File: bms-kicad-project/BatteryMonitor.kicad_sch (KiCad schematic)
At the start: 49 parts, among them J2 1053141210, U1 CD74HC4067, U2 BQ7697204PFBR

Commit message: feat: big pre-design review schematic commit
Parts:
- removed J2: 1053141210, FixedWing:CONN_SD-105314-100_10_MOL, symbol FixedWing:1053141210
- added C14: 0.1µ, FixedWing:CAP_GCJ-18_MUR, symbol FixedWing:GCJ188R72A104KA01D
- added C22, C23, C24, C25, C26, C27: 3.9n, FixedWing:G-21_MUR, symbol FixedWing:GRM2165C1H392JA01D
- added J2: 1053141308, FixedWing:CONN_SD-105314-100_08_MOL, symbol FixedWing:1053141308
- renumbered C14 to C15, C15 to C16, C16 to C17, C17 to C18, C18 to C19, C19 to C20, C20 to C21
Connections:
- net +5V: now also C14.2
- net GND: now also C14.1, C22.1, C23.1, C24.1, C25.1, C26.1, C27.1, J2.7, J2.8
- net THERM1: now reaches U2.21 (TS1)
- net THERM1: now also C22.2, J2.1
- net THERM2: now reaches U2.22 (TS2)
- net THERM2: now also C23.2, J2.2
- net THERM3: now reaches U2.23 (TS3)
- net THERM3: now also C24.2, J2.3
- net THERM4: now reaches U2.30 (DFETOFF)
- net THERM4: now also C25.2, J2.4
- net THERM5: now reaches U2.31 (DCHG)
- net THERM5: now also C26.2, J2.5
- net THERM6: now reaches U2.32 (DDSG)
- net THERM6: now also C27.2, J2.6
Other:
- moved on the sheet: C15, C16, C17, C18, C19, C20, C21, D1, NT1, R62, R63, R64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

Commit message: feat: post-design review clarity
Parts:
- added TP1, TP2, TP6, TP7: ~, TestPoint:TestPoint_Pad_D1.0mm, symbol FixedWing:TestPoint
- TP3: renamed from TP1; value TestPoint -> ~; footprint TestPoint:TestPoint_Pad_D1.5mm -> TestPoint:TestPoint_Pad_D1.0mm; symbol Connector:TestPoint -> FixedWing:TestPoint
- TP4: renamed from TP2; value TestPoint -> ~; footprint TestPoint:TestPoint_Pad_D1.5mm -> TestPoint:TestPoint_Pad_D1.0mm; symbol Connector:TestPoint -> FixedWing:TestPoint
- TP5: renamed from TP3; value TestPoint -> ~; footprint TestPoint:TestPoint_Pad_D1.5mm -> TestPoint:TestPoint_Pad_D1.0mm; symbol Connector:TestPoint -> FixedWing:TestPoint
- TP8: renamed from TP4; value TestPoint -> ~; footprint TestPoint:TestPoint_Pad_D1.5mm -> TestPoint:TestPoint_Pad_D1.0mm; symbol Connector:TestPoint -> FixedWing:TestPoint
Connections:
- net C0: now also TP2.1
- net C1: now also TP1.1
- net GND: now also TP6.1
- net at C21.1, U2.24 (REG18): now also TP7.1
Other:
- moved on the sheet: C21

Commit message: feat: I am so tired. 4-layer layout almost done
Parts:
- removed NT1: NetTie_2, NetTie:NetTie-2_SMD_Pad0.5mm, symbol Device:NetTie_2
- removed TP1, TP2, TP5, TP7, TP8: ~, TestPoint:TestPoint_Pad_D1.0mm, symbol FixedWing:TestPoint
- added TP2, TP5: 5261, FixedWing:KEYSTONE_5261, symbol FixedWing:5261
- renumbered TP3 to TP1, TP4 to TP3, TP6 to TP4
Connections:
- net GNDPWR is gone; now on net GND: R92.2, R93.2
- net -BATT: now also TP2.TP
- net GND: now also TP5.TP

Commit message: feat: biiig layout and slight design change commit
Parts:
- removed R69, R70: 10k, FixedWing:KOA_Speer-RK73H2A-0-0-MFG, symbol FixedWing:RK73H2ATTD1002F
- removed R92: 0.5m, FixedWing:RES_3920R, symbol FixedWing:PEWM3920FL500K9
- removed TP1: ~, TestPoint:TestPoint_Pad_D1.0mm, symbol FixedWing:TestPoint
- removed U1: CD74HC4067, FixedWing:DB0024A_N, symbol FixedWing:CD74HC4067
- added C14: 1µ, FixedWing:CAPC1608X90N, symbol FixedWing:GCM188R71C105KA64D
- added R65, R70, R71: 0, FixedWing:RES_CRCW_0805_VIS, symbol FixedWing:CRCW08050000Z0EA
- added R93: 1m, FixedWing:RES_5930R, symbol FixedWing:SEWF5930F1L00P9
- added U1: TMUX7208PWR, FixedWing:TSSOP16-PW_TEX, symbol FixedWing:TMUX7208PWR
- R68: renamed from R67; now not fitted
- R69: renamed from R68; now fitted
- renumbered C14 to C15, C15 to C16, C16 to C17, C17 to C18, C18 to C19, C19 to C20, C20 to C21, C21 to C22, C22 to C23, C23 to C24, C24 to C25, C25 to C26, C26 to C27, C27 to C28, R65 to R66, R66 to R67, R71 to R72, R72 to R73, R73 to R74, R74 to R75, R75 to R76, R76 to R77, R77 to R78, R78 to R79, R79 to R80, R80 to R81, R81 to R82, R82 to R83, R83 to R84, R84 to R85, R85 to R86, R86 to R87, R87 to R88, R88 to R89, R89 to R90, R90 to R91, R91 to R92, R93 to R94, R94 to R95, TP2 to TP1, TP3 to TP2, TP4 to TP3, TP5 to TP4
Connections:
- net +5V is gone; now on net +BATT: C15.2, R63.2, R66.2, R68.2
- net +BATT: now also R62.2, C14.2, U1.13 (VDD)
- net -BATT: now also R93.1
- net C10: now also U1.11 (S6)
- net C11: now also U1.10 (S7)
- net C12: now also U1.9 (S8)
- net C3: now also R71.2
- net C4: now also R70.2
- net C5: now also U1.4 (S1)
- net C6: now also U1.5 (S2)
- net C7: now also U1.6 (S3)
- net C8: now also U1.7 (S4)
- net C9: now also U1.12 (S5)
- net GND: now also C14.1, R93.2, U1.14 (GND), U1.3 (VSS); no longer R62.1
- net at R66.1, R67.1: now also U1.16 (A1)
- net at R63.1, R64.1: now also U1.1 (A0)
- net at U2.48 (VC16): now also R65.2, R70.1, R71.1
- net at R68.1, R69.1: now also U1.15 (A2)
- new net: R65.1, U1.8 (D)
- new net: R62.1, U1.2 (EN)
- no-connect marks 12 -> 6
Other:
- moved on the sheet: C15, C16, C17, C18, C19, C20, C21, C22, C23, C24, C25, C26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

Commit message: feat:bos->lax layout sesh
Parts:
- removed TP2, TP3: ~, TestPoint:TestPoint_Pad_D1.0mm, symbol FixedWing:TestPoint
- added R63: 10k, FixedWing:KOA_Speer-RK73H2A-0-0-MFG, symbol FixedWing:RK73H2ATTD1002F
- renumbered R63 to R64, R64 to R65, R65 to R66, R66 to R67, R67 to R68, R68 to R69, R69 to R70, R70 to R71, R71 to R72, R72 to R73, R73 to R74, R74 to R75, R75 to R76, R76 to R77, R77 to R78, R78 to R79, R79 to R80, R80 to R81, R81 to R82, R82 to R83, R83 to R84, R84 to R85, R85 to R86, R86 to R87, R87 to R88, R88 to R89, R89 to R90, R90 to R91, R91 to R92, R92 to R93, R93 to R94, R94 to R95, R95 to R96, TP4 to TP2
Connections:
- net GND: now also R63.1
- net at R62.1, U1.2 (EN): now also R63.2

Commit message: feat: lax -> syd layout sesh
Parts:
- removed TP1: 5261, FixedWing:KEYSTONE_5261, symbol FixedWing:5261
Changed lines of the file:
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@@
     (company "AeroNU - FixedWing")
   )
-  (junction (at 259.08 207.01) (diameter 0) (color 0 0 0 0)
-  )
   (junction (at 318.77 219.71) (diameter 0) (color 0 0 0 0)
   )
@@
     (stroke (width 0) (type default))
   )
-  (wire (pts (xy 259.08 207.01) (xy 259.08 208.28))
-    (stroke (width 0) (type default))
-  )
   (wire (pts (xy 41.91 245.11) (xy 41.91 246.38))
     (stroke (width 0) (type default))
@@
     (stroke (width 0) (type default))
   )
-  (wire (pts (xy 259.08 207.01) (xy 271.78 207.01))
-    (stroke (width 0) (type default))
-  )
   (polyline (pts (xy 29.21 138.43) (xy 44.45 138.43))
     (stroke (width 0) (type default))
@@
     (stroke (width 0) (type default))
   )
-  (wire (pts (xy 248.92 207.01) (xy 259.08 207.01))
+  (wire (pts (xy 248.92 207.01) (xy 271.78 207.01))
     (stroke (width 0) (type default))
   )
@@
         )
       )
-    )
-  )
-  (symbol (lib_id "FixedWing:5261") (at 259.08 213.36 270) (unit 1)
-    (in_bom yes) (on_board yes) (dnp no)
-    (property "Reference" "TP1" (at 256.54 215.9 90)
-      (effects (font (size 1.27 1.27)) (justify left))
-    )
-    (property "Value" "5261" (at 253.9934 210.81 0)
-      (effects (font (size 1.27 1.27)) (justify left bottom) hide)
-    )
-    (property "Footprint" "FixedWing:KEYSTONE_5261" (at 259.08 213.36 0)
-      (effects (font (size 1.27 1.27)) (justify bottom) hide)
-    )
-    (property "Datasheet" "https://www.keyelco.com/product-pdf.cfm?p=14608" (at 259.08 213.36 0)
-      (effects (font (size 1.27 1.27)) hide)
-    )
-    (property "PARTREV" "H" (at 259.08 213.36 0)
-      (effects (font (size 1.27 1.27)) (justify bottom) hide)
-    )
-    (property "STANDARD" "Manufacturer Recommendations" (at 259.08 213.36 0)
-      (effects (font (size 1.27 1.27)) (justify bottom) hide)
-    )
-    (property "SNAPEDA_PN" "5000" (at 259.08 213.36 0)
-      (effects (font (size 1.27 1.27)) (justify bottom) hide)
-    )
-    (property "MAXIMUM_PACKAGE_HEIGHT" "4.57 mm" (at 259.08 213.36 0)
-      (effects (font (size 1.27 1.27)) (justify bottom) hide)
-    )
-    (property "Manufacturer" "Keystone" (at 259.08 213.36 0)
-      (effects (font (size 1.27 1.27)) (justify bottom) hide)
-    )
-    (property "Manufacturer Part Number" "5261" (at 259.08 213.36 0)
-      (effects (font (size 1.27 1.27)) hide)
-    )
-    (pin "TP")
-    (instances
-      (project "bms-board"
-        (path "/8a7831d1-a913-4f04-8780-225d2234b41d/1e9f81b4-c330-4dde-84b6-9168ce482c70"
-          (reference "TP1") (unit 1)
-        )
-      )

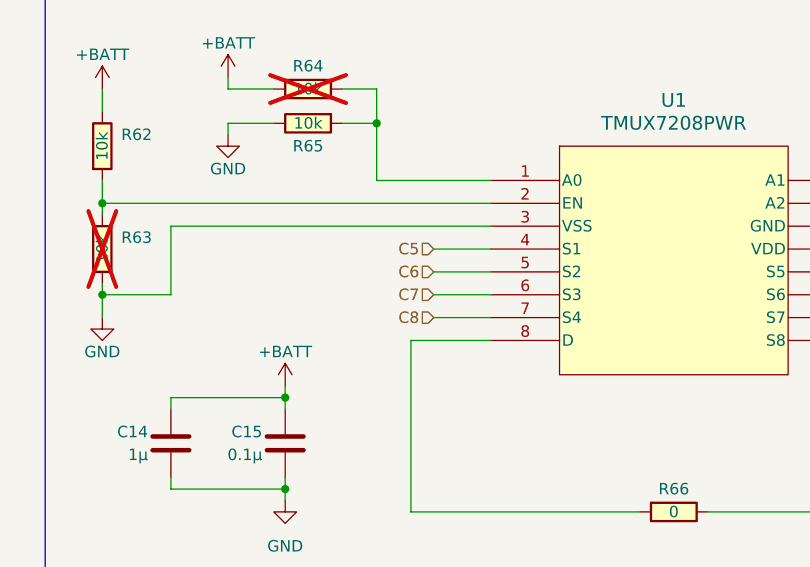
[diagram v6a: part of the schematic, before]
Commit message: feat: DRC run
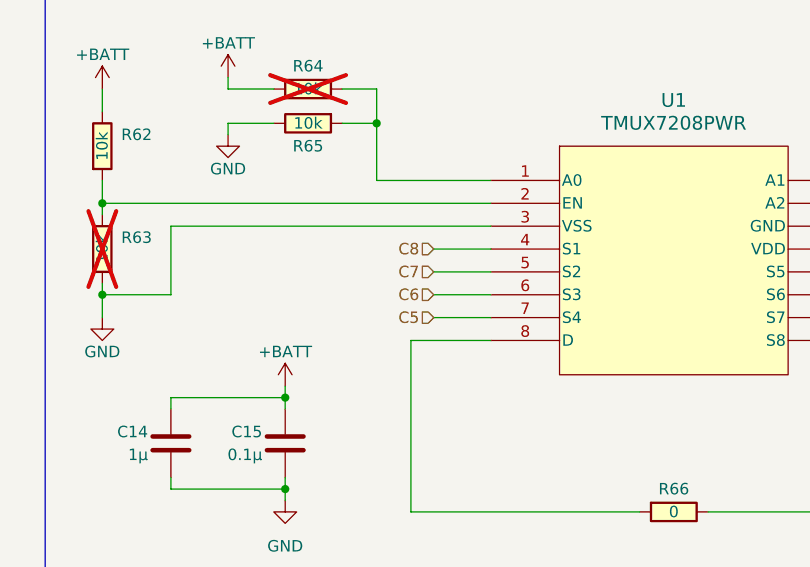
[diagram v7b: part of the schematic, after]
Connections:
- net C5: now also U1.7 (S4); no longer U1.4 (S1)
- net C6: now also U1.6 (S3); no longer U1.5 (S2)
- net C7: now also U1.5 (S2); no longer U1.6 (S3)
- net C8: now also U1.4 (S1); no longer U1.7 (S4)
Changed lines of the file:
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@@
+    (effects (font (size 1.27 1.27)) (justify right))
+  )
+  (hierarchical_label "C6" (shape input) (at 58.42 233.68 180) (fields_autoplaced)
+    (effects (font (size 1.27 1.27)) (justify right))
+  )
+  (hierarchical_label "C7" (shape input) (at 58.42 231.14 180) (fields_autoplaced)
     (effects (font (size 1.27 1.27)) (justify right))
   )
@@
     (effects (font (size 1.27 1.27)) (justify left))
   )
-  (hierarchical_label "C8" (shape input) (at 58.42 236.22 180) (fields_autoplaced)
+  (hierarchical_label "C5" (shape input) (at 58.42 236.22 180) (fields_autoplaced)
     (effects (font (size 1.27 1.27)) (justify right))
   )
@@
     (effects (font (size 1.27 1.27)) (justify right))
   )
-  (hierarchical_label "C6" (shape input) (at 58.42 231.14 180) (fields_autoplaced)
-    (effects (font (size 1.27 1.27)) (justify right))
-  )
   (hierarchical_label "C8" (shape input) (at 207.01 113.03 180) (fields_autoplaced)
-    (effects (font (size 1.27 1.27)) (justify right))
-  )
-  (hierarchical_label "C5" (shape input) (at 58.42 228.6 180) (fields_autoplaced)
     (effects (font (size 1.27 1.27)) (justify right))
   )
@@
     (effects (font (size 1.27 1.27)) (justify left))
   )
-  (hierarchical_label "C7" (shape input) (at 58.42 233.68 180) (fields_autoplaced)
+  (hierarchical_label "C8" (shape input) (at 58.42 228.6 180) (fields_autoplaced)
     (effects (font (size 1.27 1.27)) (justify right))
   )
